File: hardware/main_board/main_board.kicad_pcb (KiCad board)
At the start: 2 copper layers, 77 x 57.2 mm, 69 parts, among them J1 USB_C_Receptacle_USB2.0_16P, J2 Conn_01x03, J3 Conn_01x03, J4 Conn_02x05_Odd_Even, J5 Conn_02x10_Odd_Even, J6 2434804-1, Q1 AO3400A, Q2 AO3400A, Q3 AO3400A, Q4 AO3401A, SW1 SW_Push, SW2 SW_Push, SW3 SW_Push, U1 USBLC6-2SC6, U2 BQ24259RGER, U3 TPS7A0533PDBV, U4 STM32G0B1CBTx, U5 NHD-C0220BIZ-FSRGB

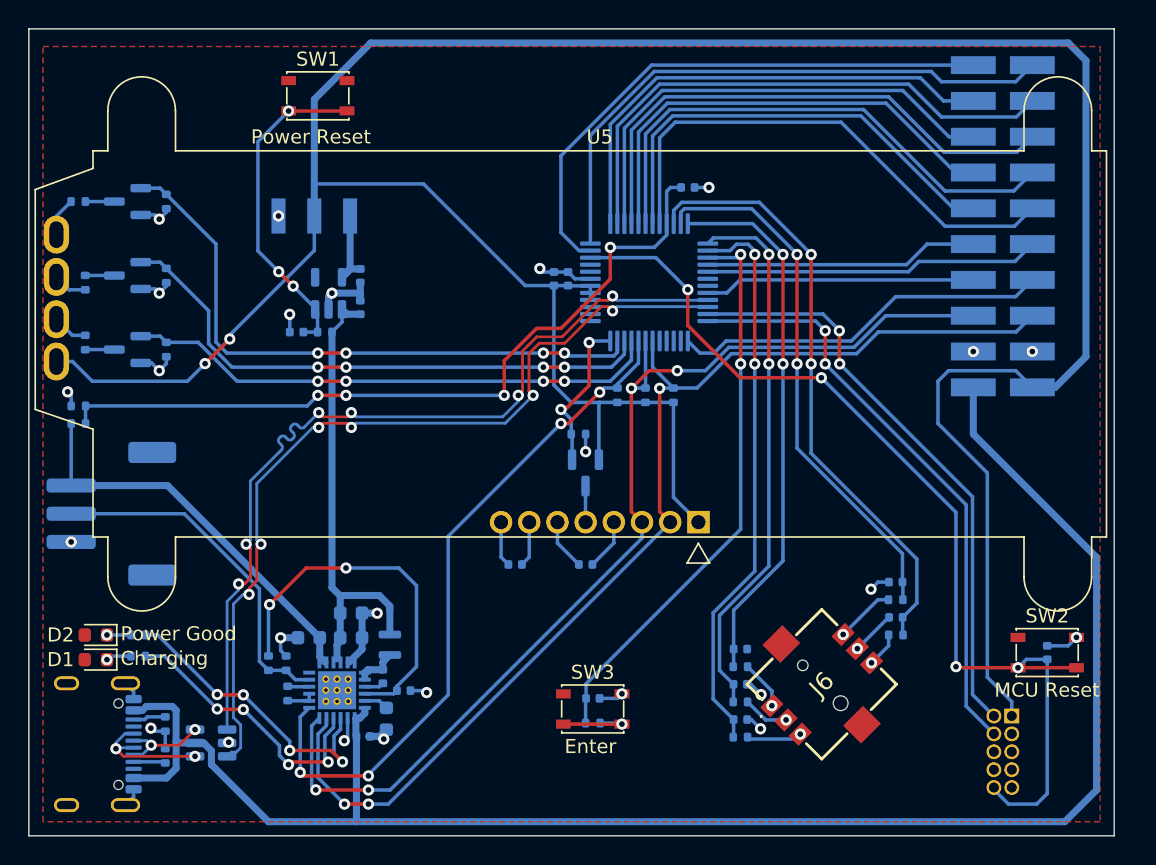
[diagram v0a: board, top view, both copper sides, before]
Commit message: Fix PCB routing errors, update LED and connector footprints
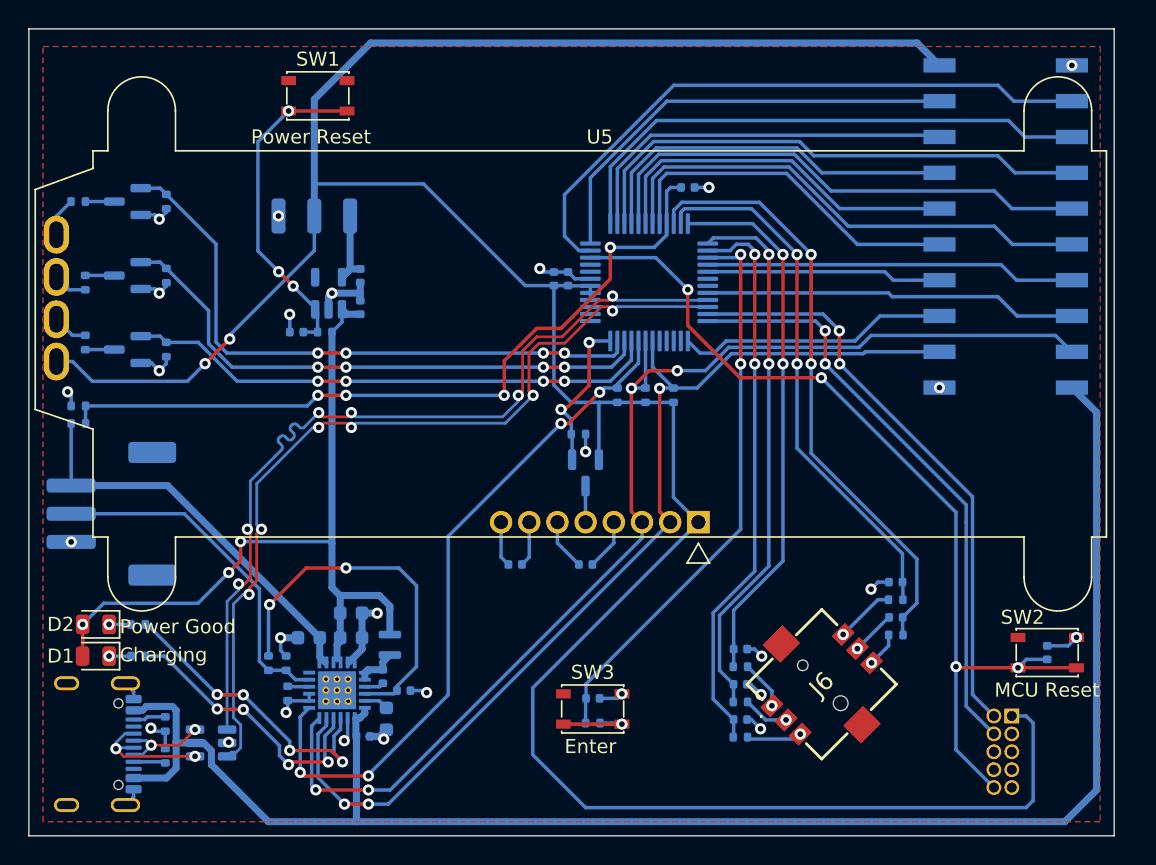
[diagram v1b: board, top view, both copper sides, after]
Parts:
- D1, D2: footprint LED_SMD:LED_0603_1608Metric -> LED_SMD:LED_0805_2012Metric
- J5: footprint Project_Footprints:SAMTEC_TSM-110-01-L-DH -> Project_Footprints:SAMTEC_SSM-110-F-DH
- R11, R12, R13, R14, R15, R16, R17, R18, R19: value 10K -> 10k
- moved J5 6.20 mm to (130.8, 56.8)
- moved D2 0.75 mm to (66.2, 85.0)
- moved R5 0.75 mm to (69.2, 85.0)
- moved D1 0.25 mm to (66.2, 87.2)
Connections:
- J5 pad 1: /MCU/PA1 -> /MCU/3V3
- J5 pad 10: /MCU/PB0 -> /MCU/PA6
- J5 pad 11: /MCU/PA9 -> /MCU/PB1
- J5 pad 12: /MCU/PA8 -> /MCU/PB0
- J5 pad 13: /MCU/PA15 -> /MCU/PA9
- J5 pad 14: /MCU/PA10 -> /MCU/PA8
- J5 pad 15: /MCU/SCL -> /MCU/PA15
- J5 pad 16: /MCU/SDA -> /MCU/PA10
- J5 pad 17: GND -> /MCU/SCL
- J5 pad 18: GND -> /MCU/SDA
- J5 pad 19: /MCU/3V3 -> GND
- J5 pad 2: /MCU/PA0 -> GND
- J5 pad 3: /MCU/PA3 -> /MCU/PA1
- J5 pad 4: /MCU/PA2 -> /MCU/PA0
- J5 pad 5: /MCU/PA5 -> /MCU/PA3
- J5 pad 6: /MCU/PA4 -> /MCU/PA2
- J5 pad 7: /MCU/PA7 -> /MCU/PA5
- J5 pad 8: /MCU/PA6 -> /MCU/PA4
- J5 pad 9: /MCU/PB1 -> /MCU/PA7
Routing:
- net /Power/SYS: track 32.7 -> 56.0 mm, vias 0 -> 3
- net /MCU/PA7: track 37.5 -> 26.1 mm
- net /MCU/PB1: track 36.6 -> 25.2 mm
- net /MCU/PA3: track 39.0 -> 27.8 mm
- net /MCU/PA5: track 38.1 -> 26.9 mm
- net /MCU/PA1: track 41.7 -> 31.7 mm
- net /MCU/PA15: track 26.9 -> 19.3 mm
- net /MCU/SCL: track 80.9 -> 73.2 mm
- net /MCU/PA10: track 19.2 -> 26.5 mm
- net /MCU/PA9: track 23.8 -> 16.7 mm
- net /MCU/SDA: track 77.6 -> 84.5 mm
- net /MCU/PA8: track 19.4 -> 26.3 mm
- net /MCU/PA0: track 40.0 -> 44.9 mm
- net /MCU/PB0: track 30.9 -> 35.6 mm
- net /MCU/PA6: track 31.9 -> 36.4 mm
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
